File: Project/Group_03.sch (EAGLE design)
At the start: 6 parts, among them J1 POWER_JACKPTH_LOCK, U1 +12v

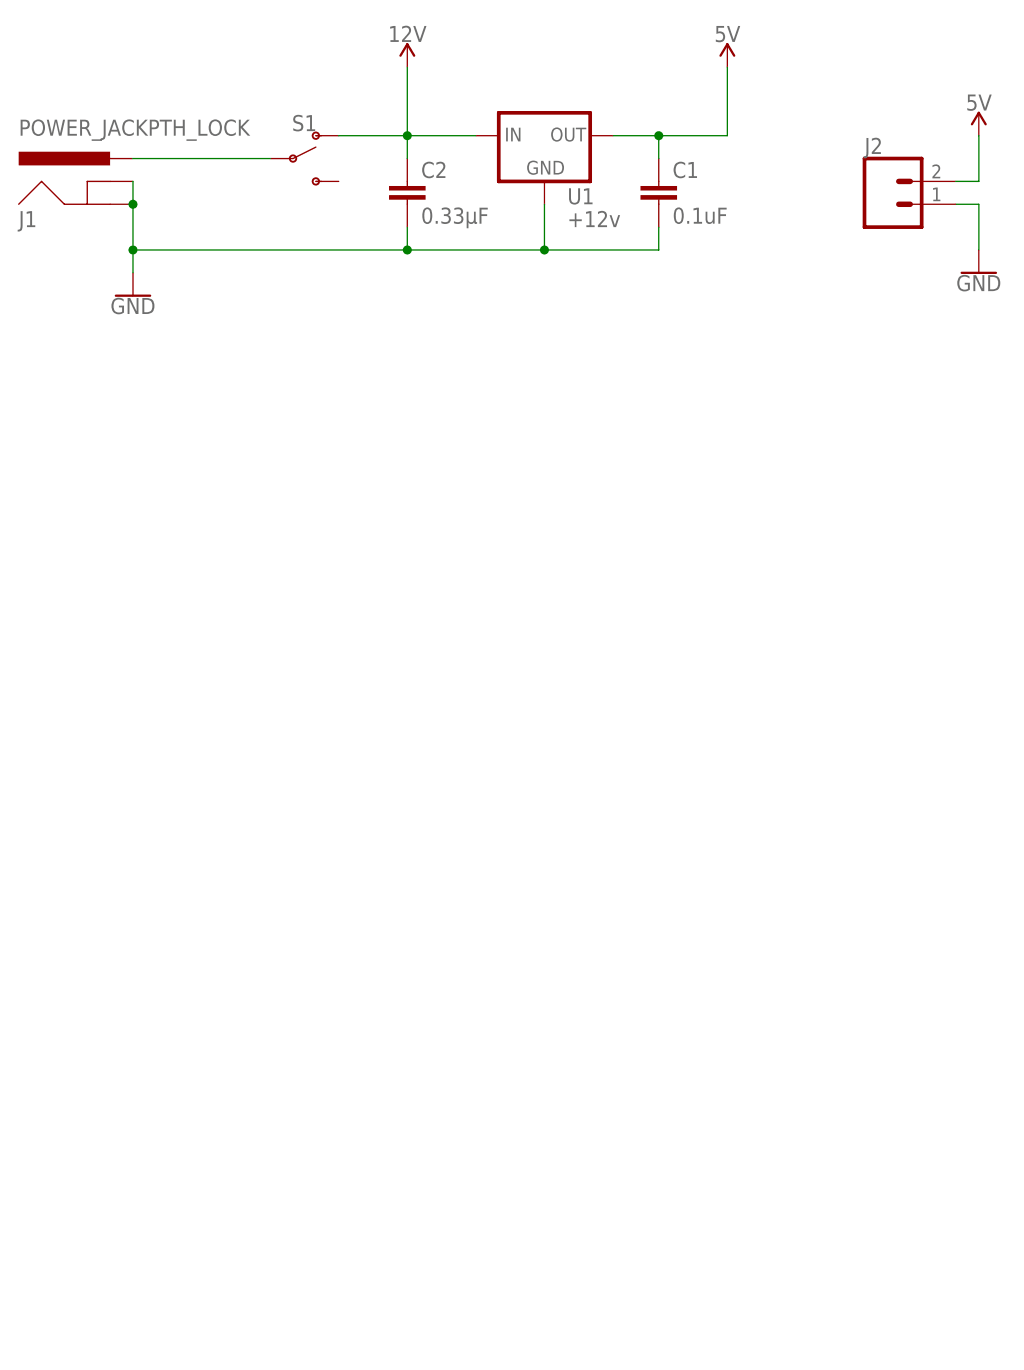
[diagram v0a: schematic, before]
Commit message: Add light and temperature sensors
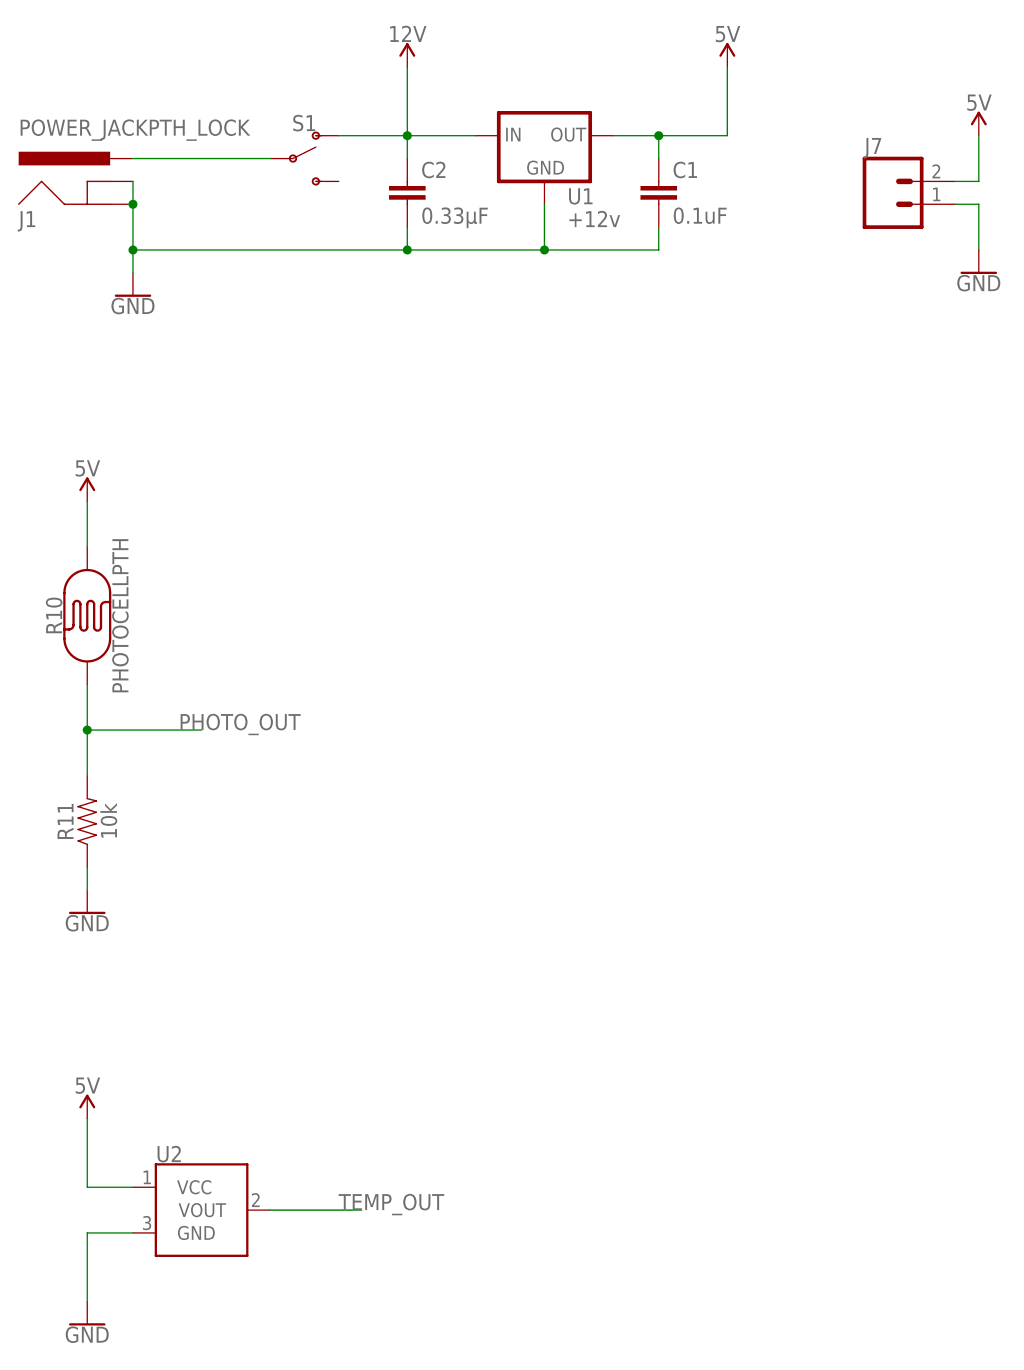
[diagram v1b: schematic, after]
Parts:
- added R10: PHOTOCELLPTH, SparkFun-Sensors:PHOTOCELLPTH
- added R11: 10k, SparkFun-Resistors:10KOHM-0603-1/10W-1%
- added U2: (no value), SparkFun-Sensors:TMP36GT9
- renumbered J2 to J7
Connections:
- new net PHOTO_OUT: R10.P$1, R11.2
- new net TEMP_OUT: U2.VOUT
- net 5V: now also R10.P$2, U2.VCC
- net GND: now also R11.1, U2.GND
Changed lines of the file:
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@@
 <part name="SUPPLY2" library="SparkFun-PowerSymbols" deviceset="12V" device=""/>
 <part name="S1" library="SparkFun-Switches" deviceset="SWITCH-SPDT" device="-PTH-11.6X4.0MM"/>
-<part name="J2" library="SparkFun-Connectors" deviceset="CONN_02" device=""/>
+<part name="J7" library="SparkFun-Connectors" deviceset="CONN_02" device=""/>
 <part name="SUPPLY3" library="SparkFun-PowerSymbols" deviceset="5V" device=""/>
 <part name="GND2" library="SparkFun-PowerSymbols" deviceset="GND" device=""/>
+<part name="R10" library="SparkFun-Sensors" deviceset="PHOTOCELL" device="PTH"/>
+<part name="R11" library="SparkFun-Resistors" deviceset="10KOHM" device="-0603-1/10W-1%" value="10k"/>
+<part name="GND3" library="SparkFun-PowerSymbols" deviceset="GND" device=""/>
+<part name="SUPPLY4" library="SparkFun-PowerSymbols" deviceset="5V" device=""/>
+<part name="SUPPLY5" library="SparkFun-PowerSymbols" deviceset="5V" device=""/>
+<part name="GND4" library="SparkFun-PowerSymbols" deviceset="GND" device=""/>
+<part name="U2" library="SparkFun-Sensors" deviceset="TMP36" device="GT9"/>
 </parts>
 <sheets>
@@
 <attribute name="VALUE" x="36.576" y="159.258" size="1.778" layer="96" font="vector" align="top-center"/>
 </instance>
-<instance part="J2" gate="G$1" x="101.6" y="157.48" smashed="yes">
+<instance part="J7" gate="G$1" x="101.6" y="157.48" smashed="yes">
 <attribute name="VALUE" x="99.06" y="152.654" size="1.778" layer="96" font="vector"/>
 <attribute name="NAME" x="99.06" y="163.068" size="1.778" layer="95" font="vector"/>
@@
 <instance part="GND2" gate="1" x="111.76" y="149.86" smashed="yes">
 <attribute name="VALUE" x="111.76" y="149.606" size="1.778" layer="96" align="top-center"/>
+</instance>
+<instance part="R10" gate="G$1" x="12.7" y="111.76" smashed="yes" rot="R90">
+<attribute name="NAME" x="9.906" y="111.76" size="1.778" layer="95" font="vector" rot="R90" align="bottom-center"/>
+<attribute name="VALUE" x="15.494" y="111.76" size="1.778" layer="96" font="vector" rot="R90" align="top-center"/>
+</instance>
+<instance part="R11" gate="G$1" x="12.7" y="88.9" smashed="yes" rot="R90">
+<attribute name="NAME" x="11.176" y="88.9" size="1.778" layer="95" font="vector" rot="R90" align="bottom-center"/>
+<attribute name="VALUE" x="14.224" y="88.9" size="1.778" layer="96" font="vector" rot="R90" align="top-center"/>
+</instance>
+<instance part="GND3" gate="1" x="12.7" y="33.02" smashed="yes">
+<attribute name="VALUE" x="12.7" y="32.766" size="1.778" layer="96" align="top-center"/>
+</instance>
+<instance part="SUPPLY4" gate="G$1" x="12.7" y="124.46" smashed="yes">
+<attribute name="VALUE" x="12.7" y="127.254" size="1.778" layer="96" align="bottom-center"/>
+</instance>
+<instance part="SUPPLY5" gate="G$1" x="12.7" y="55.88" smashed="yes">
+<attribute name="VALUE" x="12.7" y="58.674" size="1.778" layer="96" align="bottom-center"/>
+</instance>
+<instance part="GND4" gate="1" x="12.7" y="78.74" smashed="yes">
+<attribute name="VALUE" x="12.7" y="78.486" size="1.778" layer="96" align="top-center"/>
+</instance>
+<instance part="U2" gate="G$1" x="25.4" y="45.72" smashed="yes">
+<attribute name="NAME" x="20.32" y="51.054" size="1.778" layer="95" font="vector"/>
+<attribute name="VALUE" x="20.32" y="40.386" size="1.778" layer="96" font="vector" align="top-left"/>
 </instance>
 </instances>
@@
 </segment>
 <segment>
-<pinref part="J2" gate="G$1" pin="2"/>
+<pinref part="J7" gate="G$1" pin="2"/>
 <pinref part="SUPPLY3" gate="G$1" pin="5V"/>
 <wire x1="109.22" y1="160.02" x2="111.76" y2="160.02" width="0.1524" layer="91"/>
 <wire x1="111.76" y1="160.02" x2="111.76" y2="165.1" width="0.1524" layer="91"/>
 </segment>
+<segment>
+<pinref part="SUPPLY4" gate="G$1" pin="5V"/>
+<pinref part="R10" gate="G$1" pin="P$2"/>
+<wire x1="12.7" y1="124.46" x2="12.7" y2="119.38" width="0.1524" layer="91"/>
+</segment>
+<segment>
+<pinref part="U2" gate="G$1" pin="VCC"/>
+<wire x1="17.78" y1="48.26" x2="12.7" y2="48.26" width="0.1524" layer="91"/>
+<pinref part="SUPPLY5" gate="G$1" pin="5V"/>
+<wire x1="12.7" y1="48.26" x2="12.7" y2="55.88" width="0.1524" layer="91"/>
+</segment>
 </net>
 <net name="GND" class="0">
 <segment>
-<pinref part="J2" gate="G$1" pin="1"/>
+<pinref part="J7" gate="G$1" pin="1"/>
 <pinref part="GND2" gate="1" pin="GND"/>
 <wire x1="109.22" y1="157.48" x2="111.76" y2="157.48" width="0.1524" layer="91"/>
@@
 <junction x="63.5" y="152.4"/>
 </segment>
+<segment>
+<pinref part="R11" gate="G$1" pin="1"/>
+<pinref part="GND4" gate="1" pin="GND"/>
+<wire x1="12.7" y1="83.82" x2="12.7" y2="81.28" width="0.1524" layer="91"/>
+</segment>
+<segment>
+<pinref part="U2" gate="G$1" pin="GND"/>
+<wire x1="17.78" y1="43.18" x2="12.7" y2="43.18" width="0.1524" layer="91"/>
+<pinref part="GND3" gate="1" pin="GND"/>
+<wire x1="12.7" y1="43.18" x2="12.7" y2="35.56" width="0.1524" layer="91"/>
+</segment>
 </net>
+<net name="PHOTO_OUT" class="0">
+<segment>
+<pinref part="R10" gate="G$1" pin="P$1"/>
+<pinref part="R11" gate="G$1" pin="2"/>
+<wire x1="12.7" y1="104.14" x2="12.7" y2="99.06" width="0.1524" layer="91"/>
+<junction x="12.7" y="99.06"/>
+<wire x1="12.7" y1="99.06" x2="12.7" y2="93.98" width="0.1524" layer="91"/>
+<wire x1="12.7" y1="99.06" x2="25.4" y2="99.06" width="0.1524" layer="91"/>
+<label x="22.86" y="99.06" size="1.778" layer="95"/>
+</segment>
+</net>
+<net name="TEMP_OUT" class="0">
+<segment>
+<pinref part="U2" gate="G$1" pin="VOUT"/>
+<wire x1="33.02" y1="45.72" x2="43.18" y2="45.72" width="0.1524" layer="91"/>
+<label x="40.64" y="45.72" size="1.778" layer="95"/>
+</segment>
+</net>

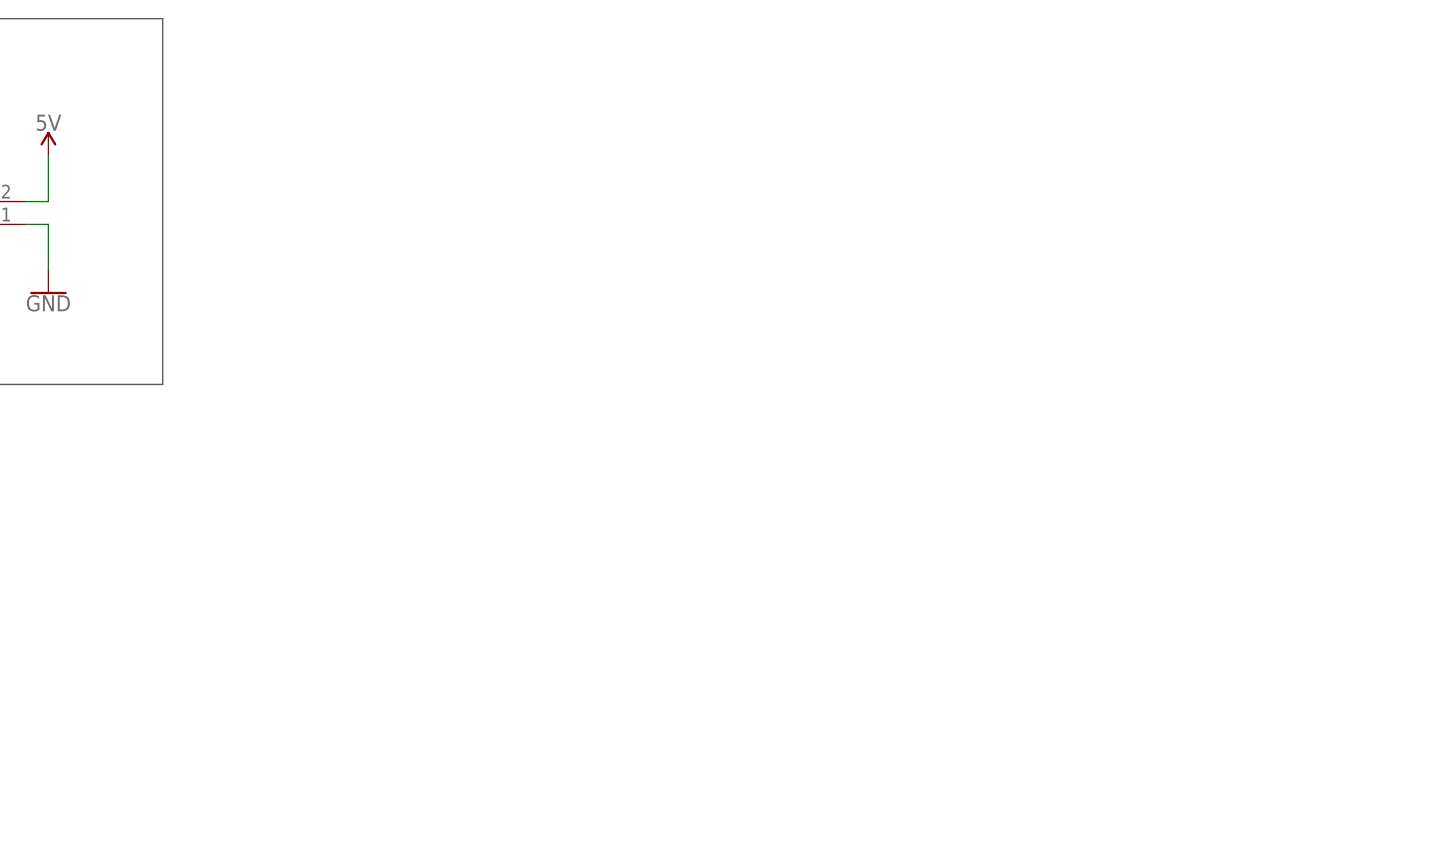
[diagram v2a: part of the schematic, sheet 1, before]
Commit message: Add 4-Channel I2C
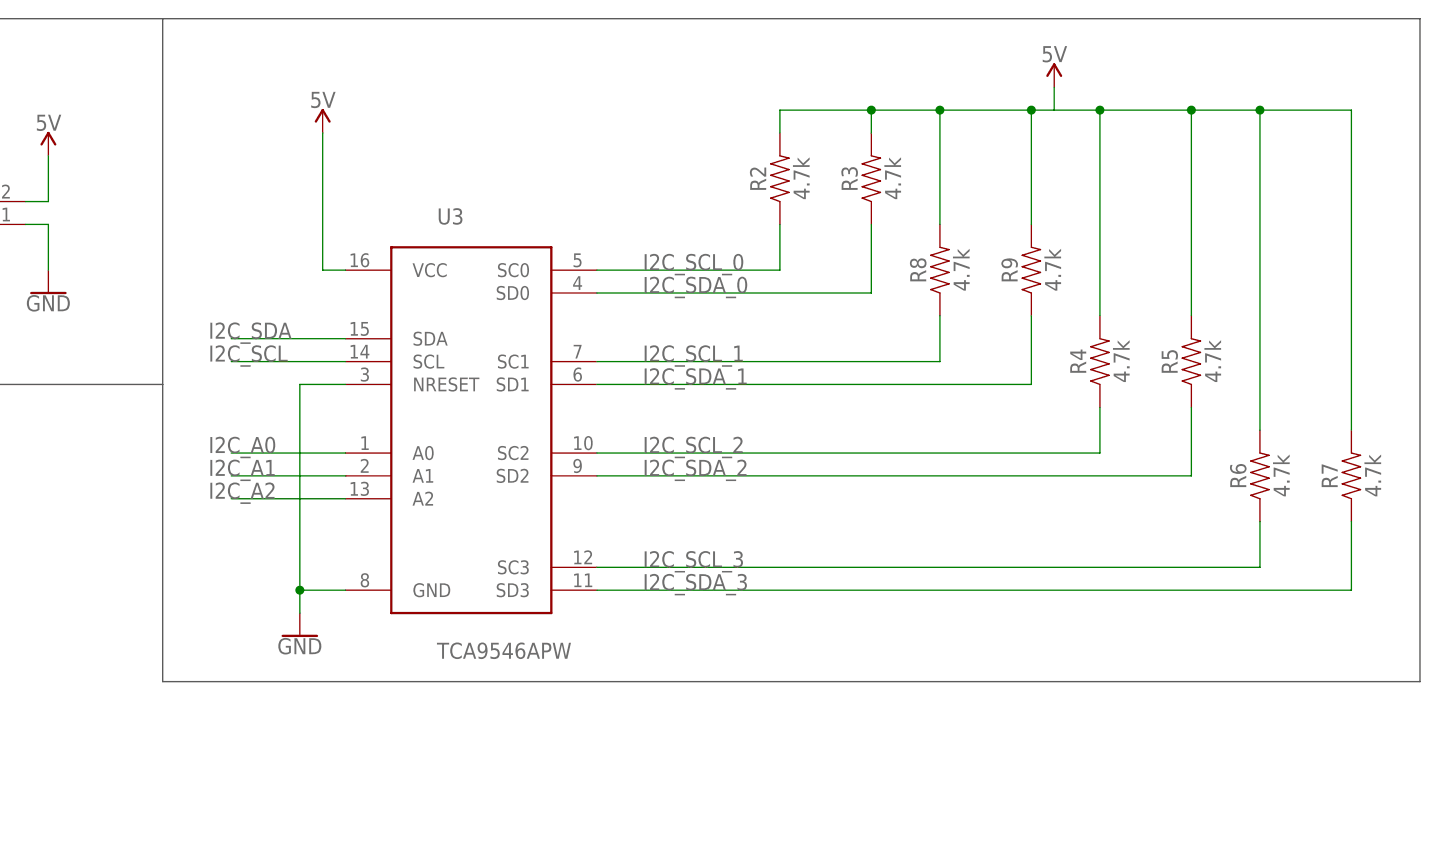
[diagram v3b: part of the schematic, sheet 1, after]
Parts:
- added R2, R3, R4, R5, R6, R7, R8, R9: 4.7k, SparkFun-Resistors:4.7KOHM-0603-1/10W-1%
- added U3: TCA9546APW, Group_03_Library:TCA9546APW
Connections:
- new net I2C_A0: U3.A0
- new net I2C_A1: U3.A1
- new net I2C_A2: U3.A2
- new net I2C_SCL: U3.SCL
- new net I2C_SCL_0: R2.1, U3.SC0
- new net I2C_SCL_1: R8.1, U3.SC1
- new net I2C_SCL_2: R4.1, U3.SC2
- new net I2C_SCL_3: R6.1, U3.SC3
- new net I2C_SDA: U3.SDA
- new net I2C_SDA_0: R3.1, U3.SD0
- new net I2C_SDA_1: R9.1, U3.SD1
- new net I2C_SDA_2: R5.1, U3.SD2
- new net I2C_SDA_3: R7.1, U3.SD3
- new net N$10: R2.2, R3.2, R4.2, R5.2, R6.2, R7.2, R8.2, R9.2
- net 5V: now also U3.VCC
- net GND: now also U3.GND, U3.NRESET
